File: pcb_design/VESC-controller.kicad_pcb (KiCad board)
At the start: 4 copper layers, 160 x 90 mm, 257 parts, among them J1 GATE_DRIVER_CONN_U, J2 GATE_DRIVER_CONN_V, J3 GATE_DRIVER_CONN_W, J4 micro USB, J5 ACCEL, J6 REGEN, J7 12V, J8 V_BUS, J9 SWD, P1 HALL/Encoder, P101 CANBUS, P2 Resolver, P3 PWR_COMM, Q1 BSC340N08, U1 STM32F40X_LQFP64, U10 LM2903-SO8, U11 LM3488, U12 OPA2376AID, U13 LM1117IMP-v.v, U14 OPA2376AID, U16 OPA2376AID, U17 LM2903-SO8, U2 ISO1050, U3 OPA2376AID, U4 LM2903-SO8, U5 7400-TSSOP, U6 SN74ALVC08PWR, U7 SN74ALVC08PWR, U8 SN74AUP1G74, U9 LM22676QTJ-5.0, X2 ABM3B - 8MHz

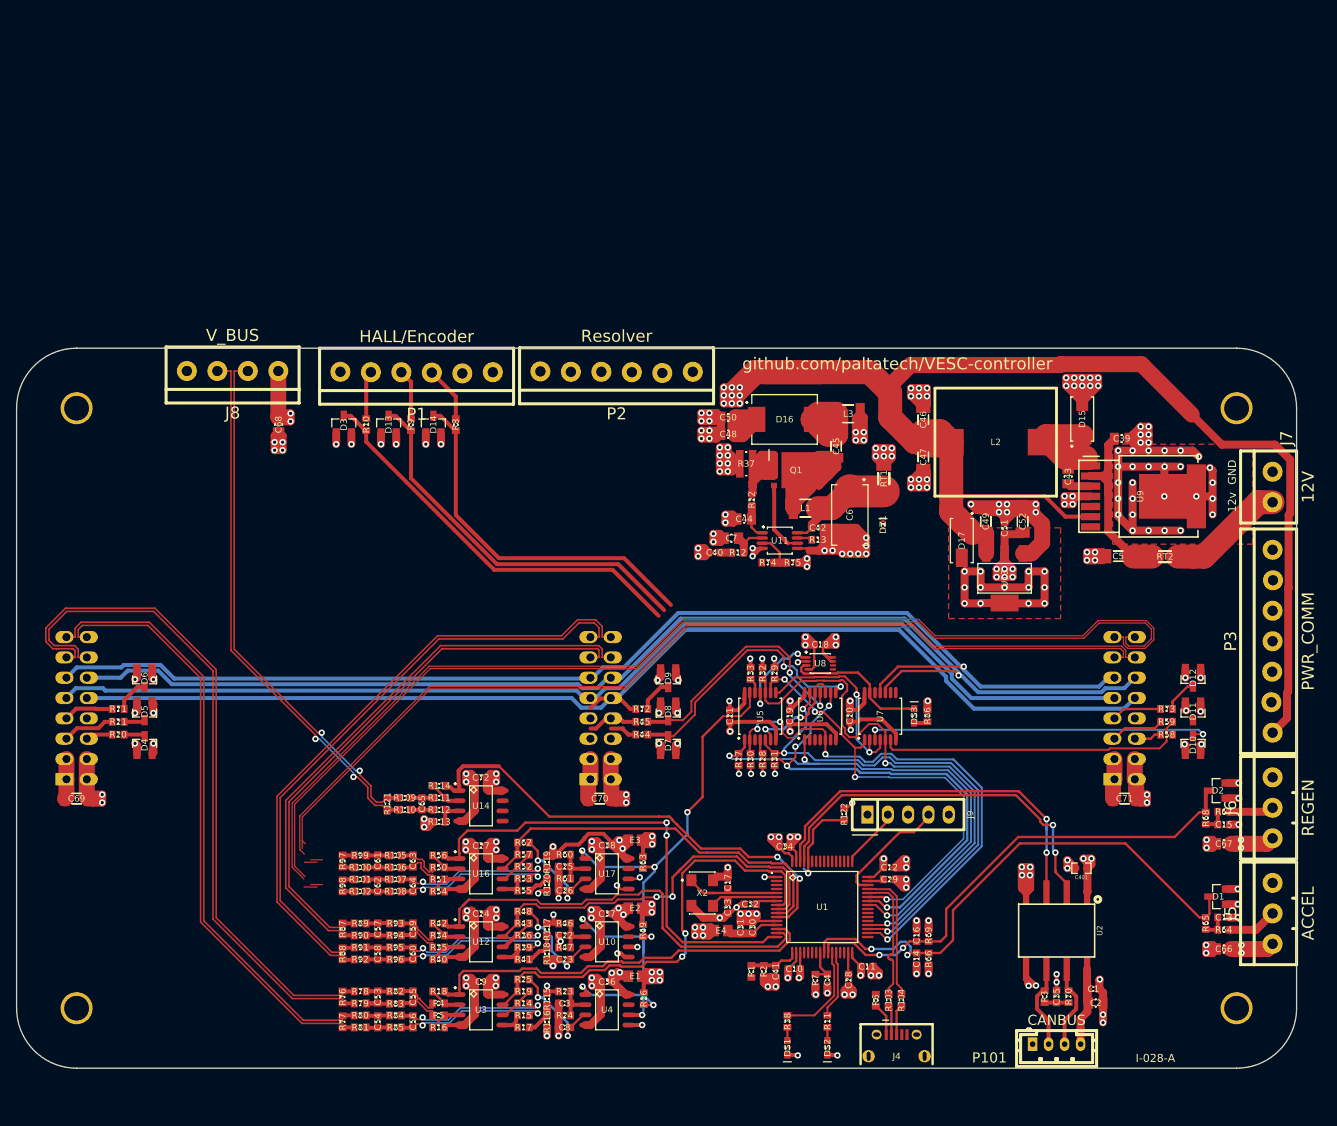
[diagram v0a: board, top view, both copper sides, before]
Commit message: Added reverse polarity protection on the isolated side of CON connector. Also, more layout
Signed-off-by: Marcos Chaparro <mchaparro@paltatech.com>
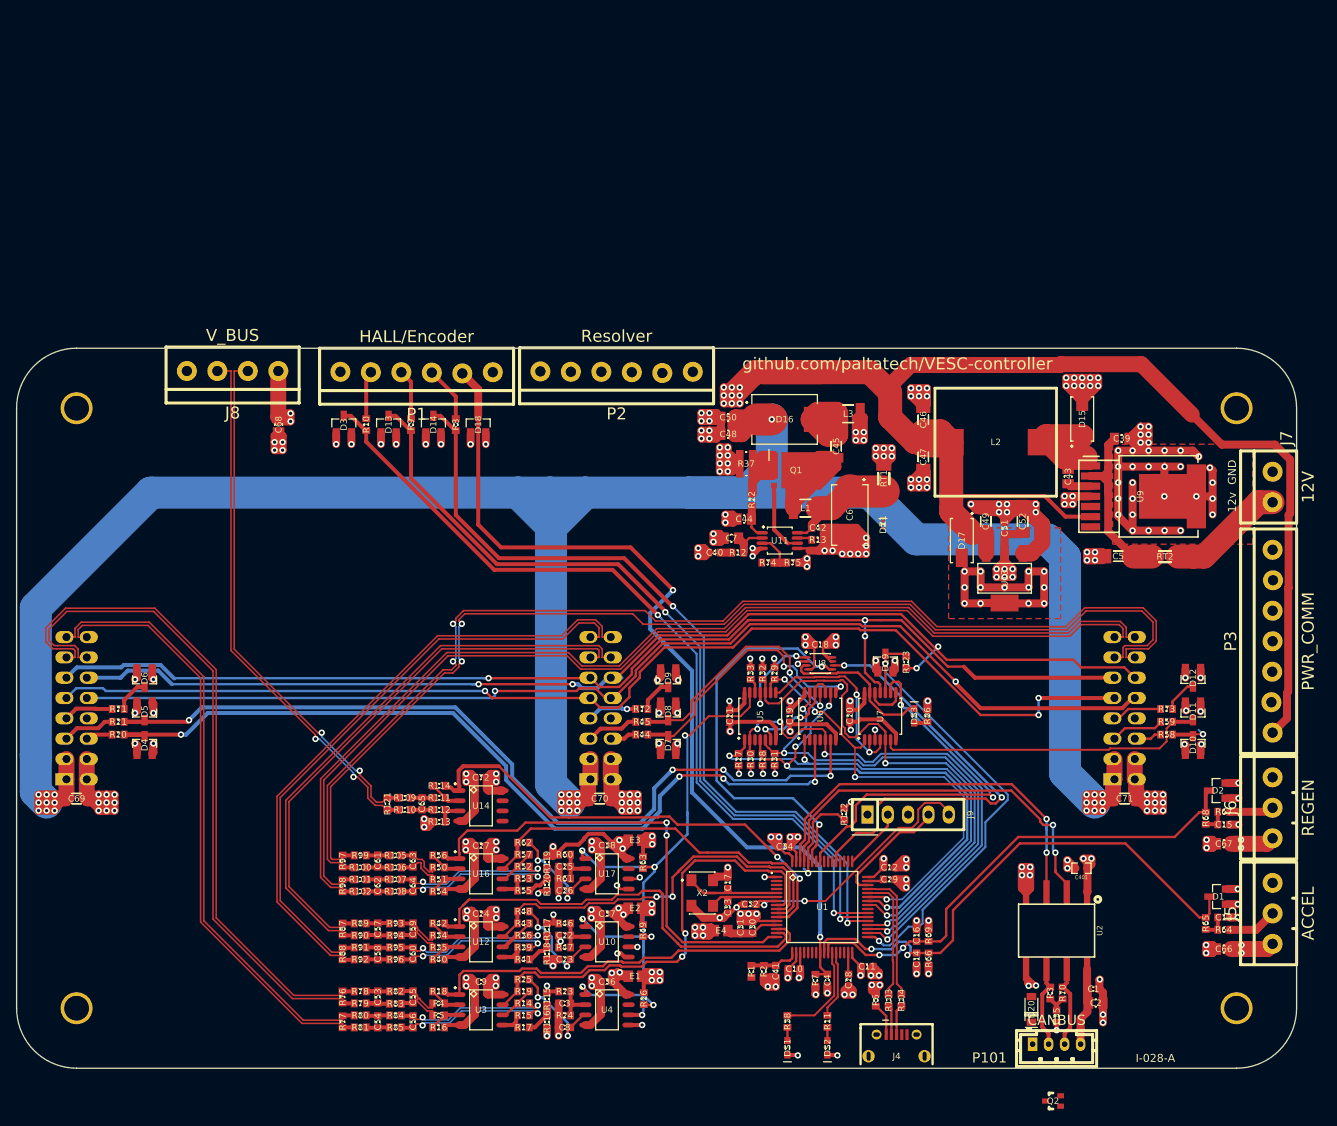
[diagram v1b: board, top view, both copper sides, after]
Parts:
- added D18: BAT54S, smd-semi:SOT-23, F.Cu at (-22.3, -35.5)
- added D19: BAT54S, smd-semi:SOT-23, F.Cu at (28.6, -5.70)
- added D20: MBR0540, smd-semi:SOD-123, F.Cu at (46.9, 37.6)
- added Q2: 2N7002PW, smd-semi:SC-70, F.Cu at (49.5, 49.1)
- added R123: 22R, IPC7351-Nominal:RESC1608X50, F.Cu at (31.2, -5.75)
- moved C35 2.45 mm to (50.0, 38.5), turned to 90 degrees
- moved R70 0.87 mm to (50.8, 35.6)
- moved R3 0.83 mm to (49.2, 35.6)
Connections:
- C1 pad 2: /Isolated CAN/GND_CAN -> ISOGND
- C2 pad 2: /Isolated CAN/GND_CAN -> ISOGND
- C35 pad 1: /Isolated CAN/GND_CAN -> ISOGND
- U1 pad 33: ~FAULT -> /STM32F4/~FAULT
- U2 pad 5: /Isolated CAN/GND_CAN -> ISOGND
- U7 pad 10: ~FAULT -> /STM32F4/~FAULT
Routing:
- net +24: track 23.4 -> 344.3 mm, vias 0 -> 28
- net /Filters/TEMP_IN: track 4.59 -> 111.3 mm, vias 0 -> 2
- net /conditioning U/PWM_B: track 2.63 -> 108.4 mm, vias 0 -> 4
- net /Supervisor/PWM_GUT: track 2.64 -> 106.9 mm, vias 0 -> 4
- net +5: track 335.5 -> 403.3 mm, vias 15 -> 17
- net /STM32F4/~FAULT: track 0.00 -> 59.9 mm, vias 0 -> 2
- net /Filters/HALL1_OUT: track 45.7 -> 101.6 mm, vias 0 -> 2
- net /Filters/HALL2_OUT: track 48.0 -> 103.6 mm, vias 0 -> 2
- net /Filters/HALL3_OUT: track 50.5 -> 105.5 mm, vias 0 -> 2
- net /Supervisor/CLR_OC_Fault: track 0.00 -> 54.7 mm, vias 0 -> 2
- net /Supervisor/OC_Fault: track 0.00 -> 50.1 mm, vias 0 -> 2
- net /STM32F4/~DRIVER_RESET: track 0.00 -> 48.7 mm, vias 0 -> 2
- net /Supervisor/PWM_GWT: track 43.8 -> 6.01 mm
- net GND: track 571.5 -> 604.8 mm, vias 207 -> 230
- net /STM32F4/NRST: track 2.72 -> 33.8 mm, vias 0 -> 2
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
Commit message: Resolver routed using push pull buffer
Signed-off-by: Marcos Chaparro <mchaparro@paltatech.com>
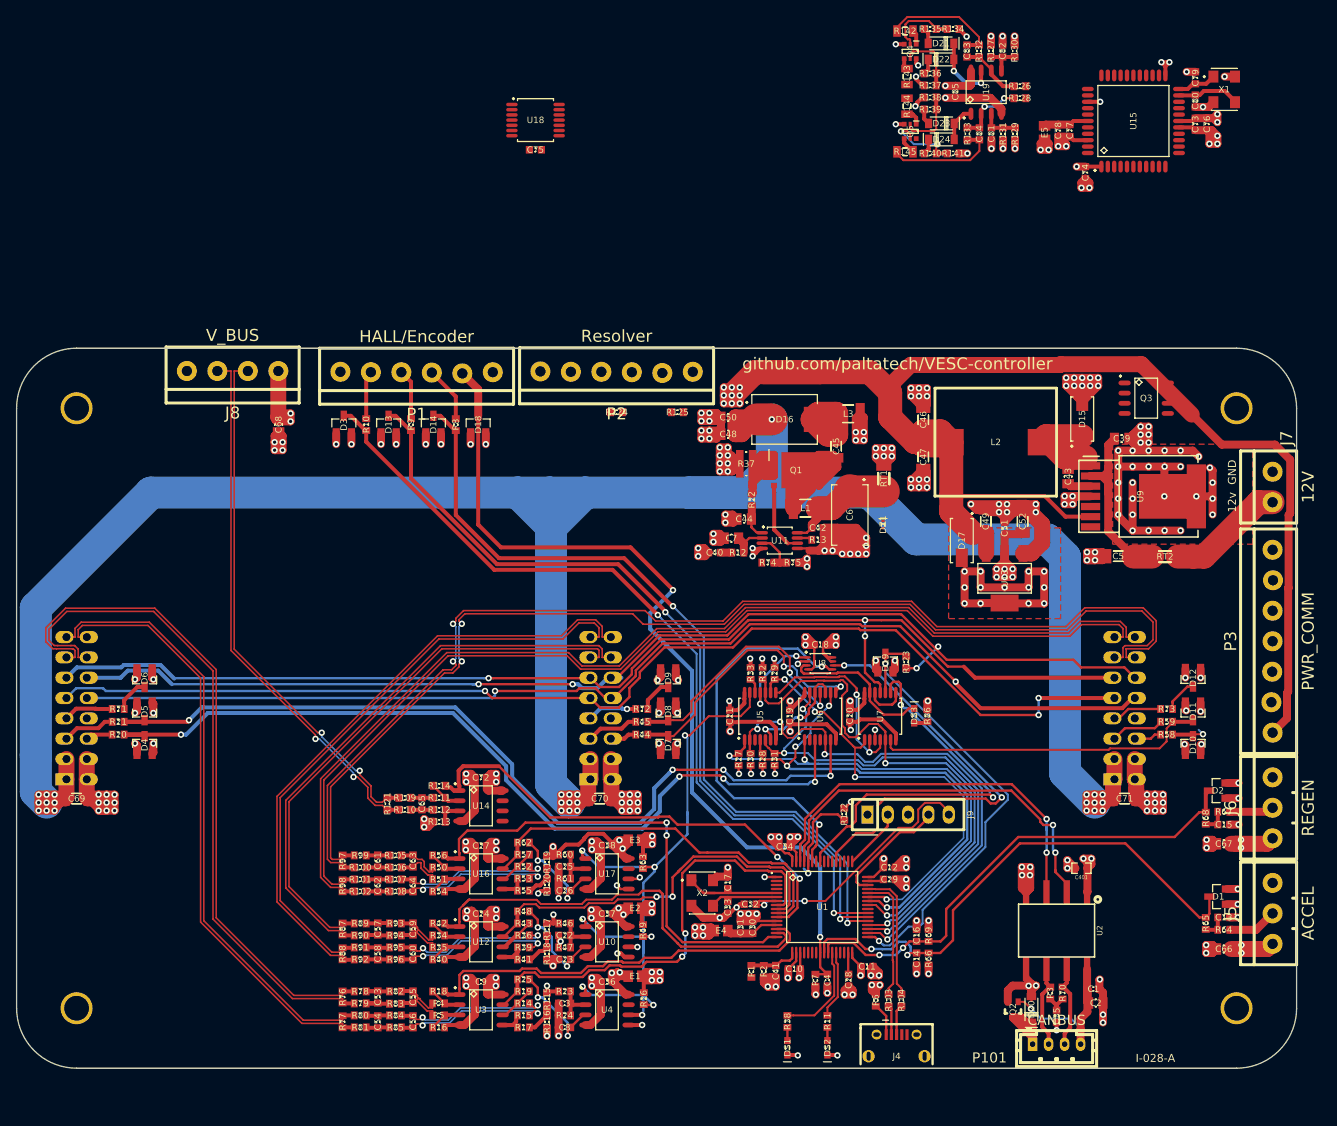
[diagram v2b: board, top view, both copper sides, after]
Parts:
- added C73: 100nF, IPC7351-Nominal:CAPC1608X55, F.Cu at (67.3, -73.0)
- added C74: 100nF, IPC7351-Nominal:CAPC1608X55, F.Cu at (53.6, -67.0)
- added C75: 100nF, IPC7351-Nominal:CAPC1608X55, F.Cu at (-15.2, -69.8)
- added C76: 4.7uF, IPC7351-Nominal:CAPC1608X55, F.Cu at (68.8, -73.0)
- added C77: 100nF, IPC7351-Nominal:CAPC1608X55, F.Cu at (51.6, -72.2)
- added C78: 4.7uF, IPC7351-Nominal:CAPC1608X55, F.Cu at (50.2, -72.2)
- added C79: 15p, IPC7351-Nominal:CAPC1608X55, F.Cu at (67.3, -78.8)
- added C80: 15p, IPC7351-Nominal:CAPC1608X55, F.Cu at (67.3, -75.9)
- added C81: 100nF, IPC7351-Nominal:CAPC1608X55, F.Cu at (41.9, -71.8)
- added C82: 100nF, IPC7351-Nominal:CAPC1608X55, F.Cu at (43.2, -82.2)
- added C83: 100nF, IPC7351-Nominal:CAPC1608X55, F.Cu at (38.8, -82.2)
- added C84: 100nF, IPC7351-Nominal:CAPC1608X55, F.Cu at (40.4, -71.8)
- added C85: 100nF, IPC7351-Nominal:CAPC1608X55, F.Cu at (37.4, -77.0)
- added D21: 1N4148W, smd-semi:SOD-123, F.Cu at (35.5, -83.1)
- added D22: 1N4148W, smd-semi:SOD-123, F.Cu at (35.5, -81.1)
- added D23: 1N4148W, smd-semi:SOD-123, F.Cu at (35.6, -73.1)
- added D24: 1N4148W, smd-semi:SOD-123, F.Cu at (35.6, -71.1)
- added E5: BEAD-220ohm@100khz, IPC7351-Nominal:INDC2012X130, F.Cu at (48.5, -72.0)
- added Q3: AO4805, IPC7351-Nominal:SOIC127P600X175-8, F.Cu at (61.2, -38.8)
- added Q4: BC846BPDW1, smd-semi:SOT-363, F.Cu at (31.7, -82.1)
- added Q5: BC846BPDW1, smd-semi:SOT-363, F.Cu at (31.7, -72.1)
- added R124: 68k, IPC7351-Nominal:RESC1608X50, F.Cu at (-5.00, -37.0)
- added R125: 68k, IPC7351-Nominal:RESC1608X50, F.Cu at (2.60, -37.0)
- added R126: 10k, IPC7351-Nominal:RESC1608X50, F.Cu at (45.4, -77.8)
- added R127: 10k, IPC7351-Nominal:RESC1608X50, F.Cu at (41.8, -82.2)
- added R128: 10k, IPC7351-Nominal:RESC1608X50, F.Cu at (45.4, -76.2)
- added R129: 10k, IPC7351-Nominal:RESC1608X50, F.Cu at (44.8, -71.8)
- added R130: 10k, IPC7351-Nominal:RESC1608X50, F.Cu at (44.8, -82.2)
- added R131: 10k, IPC7351-Nominal:RESC1608X50, F.Cu at (43.3, -71.8)
- added R132: 10k, IPC7351-Nominal:RESC1608X50, F.Cu at (40.3, -82.2)
- added R133: 10k, IPC7351-Nominal:RESC1608X50, F.Cu at (38.9, -71.8)
- added R134: 2.2k, IPC7351-Nominal:RESC1608X50, F.Cu at (37.0, -84.9)
- added R135: 3.3R, IPC7351-Nominal:RESC1608X50, F.Cu at (34.2, -84.9)
- added R136: 3.3R, IPC7351-Nominal:RESC1608X50, F.Cu at (34.2, -79.3)
- added R137: 2.2k, IPC7351-Nominal:RESC1608X50, F.Cu at (34.2, -77.8)
- added R138: 2.2k, IPC7351-Nominal:RESC1608X50, F.Cu at (34.2, -76.3)
- added R139: 3.3R, IPC7351-Nominal:RESC1608X50, F.Cu at (34.2, -74.8)
- added R140: 3.3R, IPC7351-Nominal:RESC1608X50, F.Cu at (34.2, -69.3)
- added R141: 2.2k, IPC7351-Nominal:RESC1608X50, F.Cu at (37.0, -69.3)
- added R142: 4.7R, IPC7351-Nominal:RESC2012X50, F.Cu at (31.1, -84.7)
- added R143: 4.7R, IPC7351-Nominal:RESC2012X50, F.Cu at (31.3, -79.0)
- added R144: 4.7R, IPC7351-Nominal:RESC2012X50, F.Cu at (31.3, -75.2)
- added R145: 4.7R, IPC7351-Nominal:RESC2012X50, F.Cu at (31.1, -69.5)
- added U15: AD2S1205, IPC7351-Nominal:QFP80P1200X1200X160-44, F.Cu at (59.6, -73.4)
- added U18: SN74ALVC08PWR, IPC7351-Nominal:SOP65P640X110-14, F.Cu at (-15.1, -73.5)
- added U19: OPA2376AID, IPC7351-Nominal:SOIC127P600X175-8, F.Cu at (41.2, -77.0)
- added X1: ABM3B - 8MHz, IPC7351-Nominal:OSCCC320X500X150, F.Cu at (71.0, -77.3)
- moved Q2 12.5 mm to (44.5, 37.6), turned to 270 degrees
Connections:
- RT1 pad 2: /Power/12v_in -> Net-(Q3-Pad5)
- RT2 pad 2: /Power/12v_in -> Net-(Q3-Pad5)
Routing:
- net GND: track 604.8 -> 652.7 mm, vias 230 -> 252
- net +5: track 403.3 -> 419.5 mm, vias 17 -> 24
- net /resolver/EXC+: track 0.00 -> 14.8 mm
- net /resolver/EXC-: track 0.00 -> 14.3 mm
- net /Isolated CAN/5v_CAN: track 11.7 -> 22.7 mm, vias 0 -> 1
- net Net-(Q5-Pad5): track 0.00 -> 9.62 mm, vias 0 -> 2
- net /Isolated CAN/GND_CAN: track 0.00 -> 9.60 mm
- net Net-(D21-Pad1): track 0.00 -> 9.03 mm, vias 0 -> 2
- net +12: track 0.00 -> 9.01 mm, vias 0 -> 4
- net Net-(Q4-Pad2): track 0.00 -> 8.71 mm
- net Net-(C84-Pad2): track 0.00 -> 8.50 mm, vias 0 -> 2
- net ISOGND: track 13.4 -> 21.7 mm
- net Net-(Q4-Pad5): track 0.00 -> 7.98 mm
- net Net-(Q5-Pad2): track 0.00 -> 7.97 mm
- net Net-(C80-Pad1): track 0.00 -> 7.88 mm
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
